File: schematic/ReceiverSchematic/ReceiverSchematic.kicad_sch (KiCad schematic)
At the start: 9 parts, among them Q1 BC547 (or similar NPN), Q2 S8550 (or similar PNP), U1 ESP32-DevKitC, U2 Ender 3 LCD (EXP3)

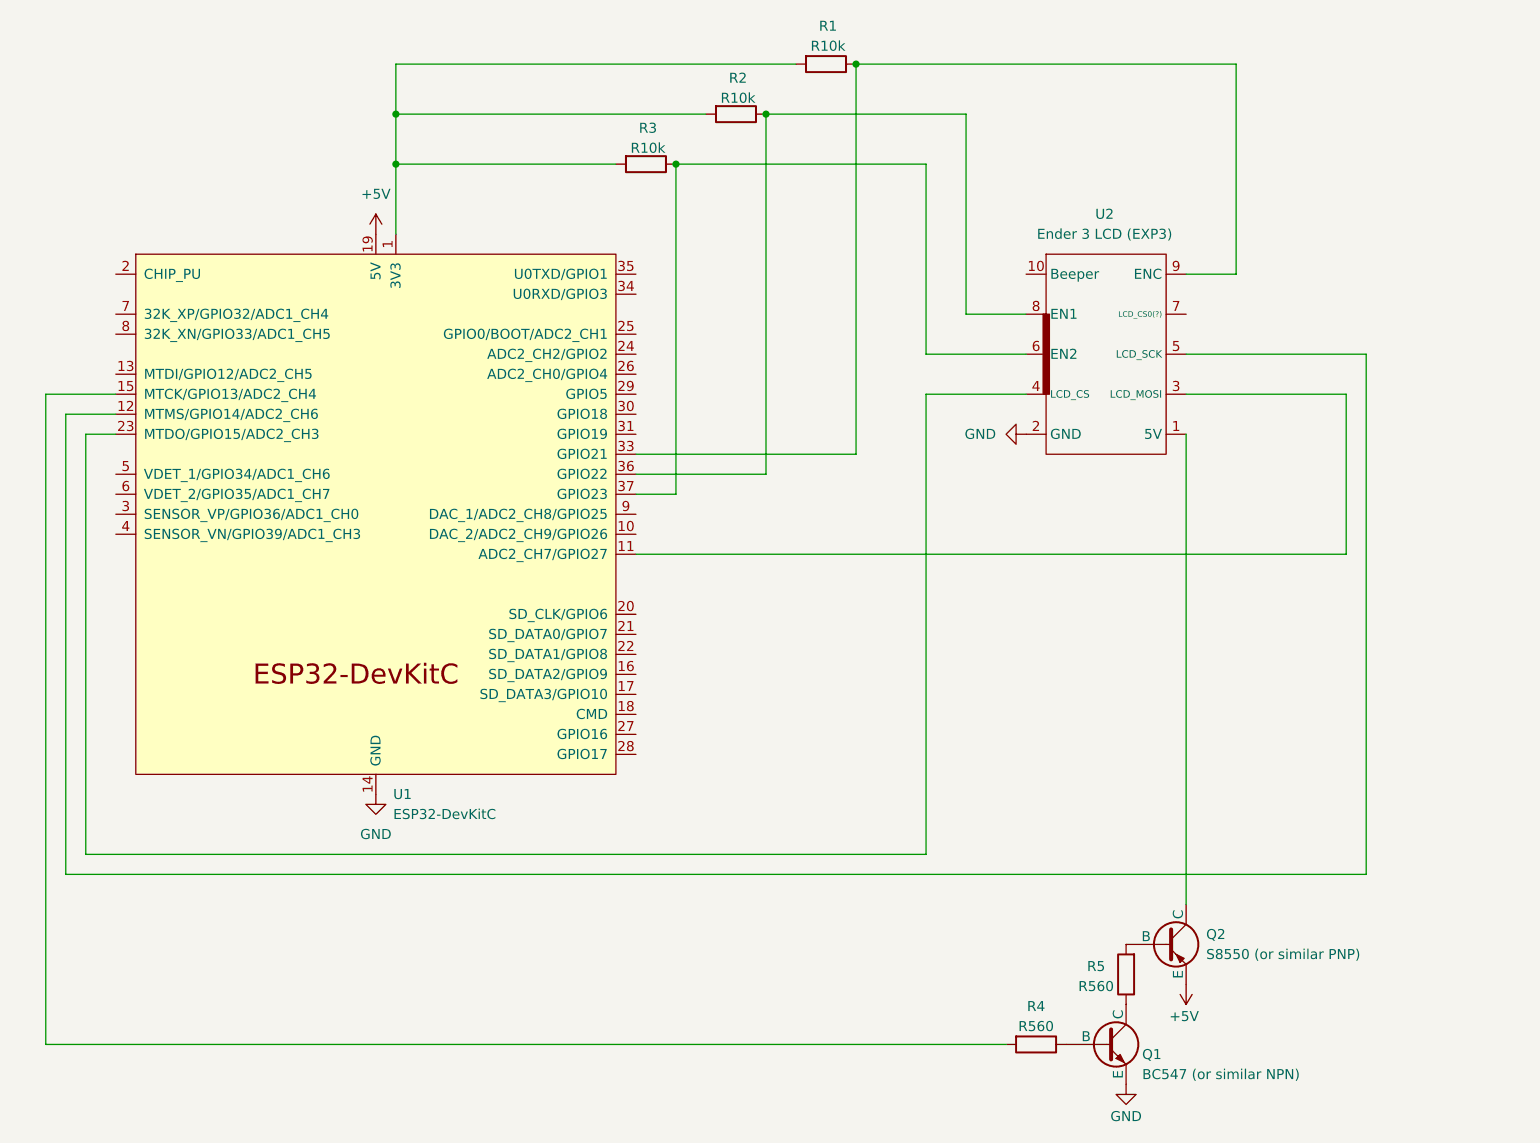
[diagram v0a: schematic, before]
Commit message: add LED ring to receiver schematic and CAD
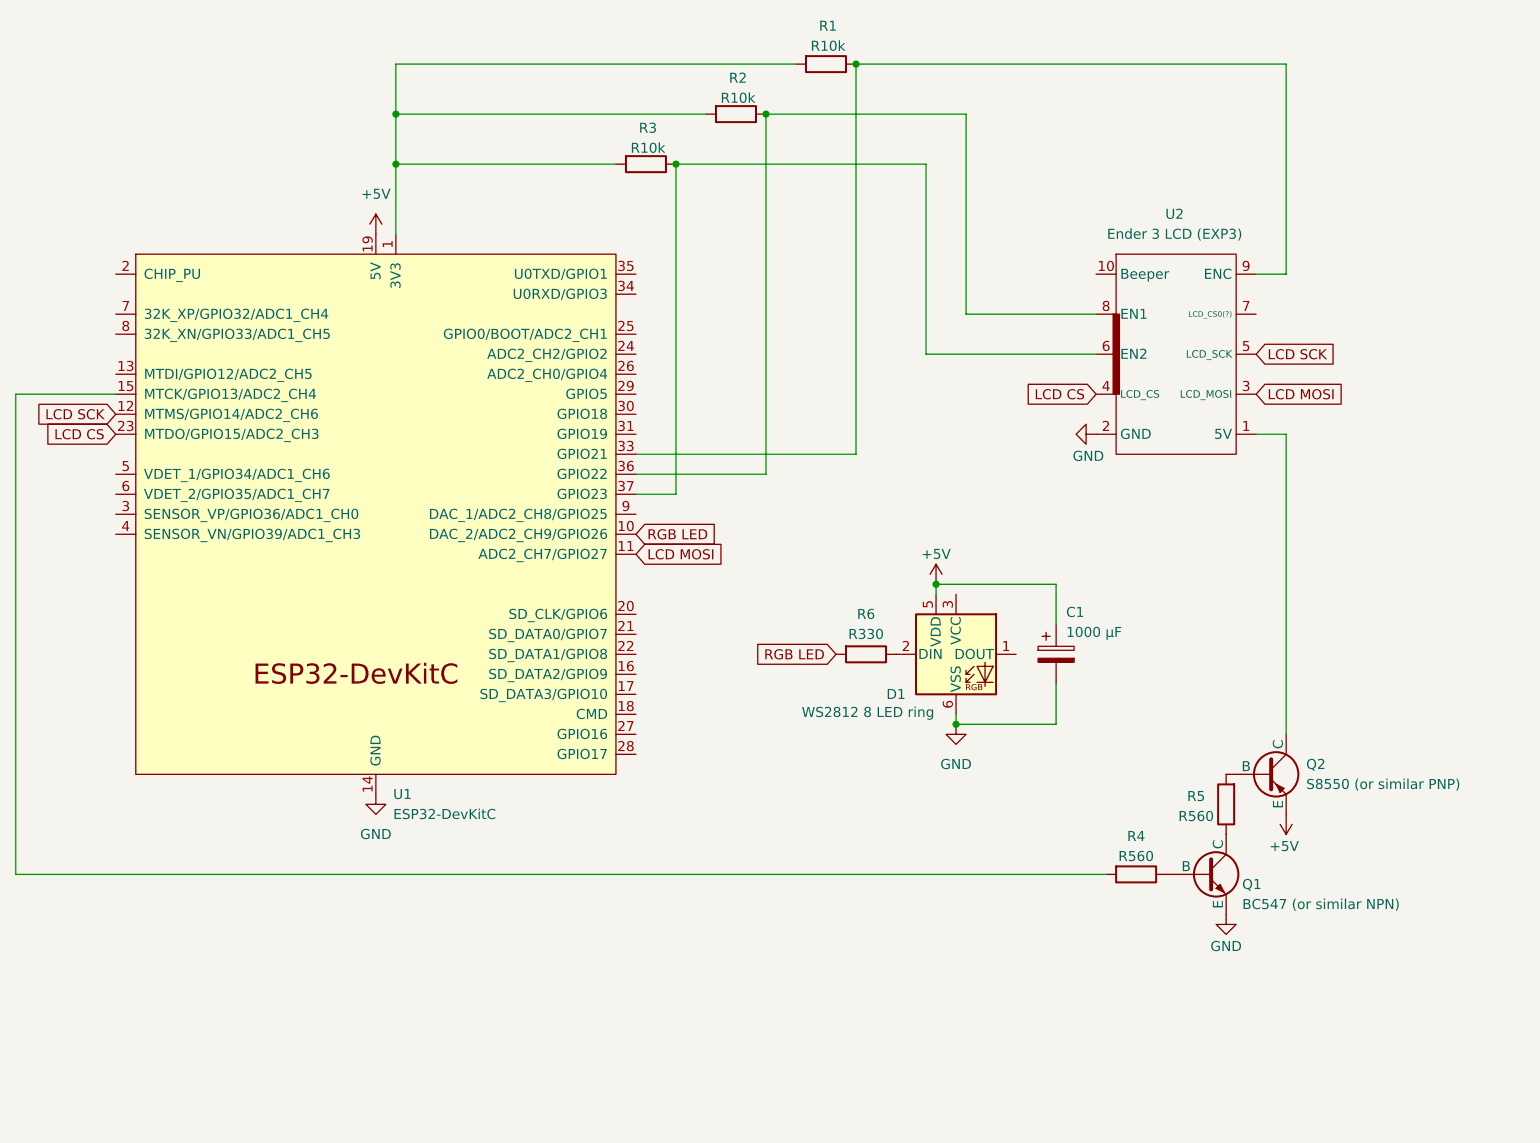
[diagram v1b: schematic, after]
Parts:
- added C1: 1000 μF, symbol Device:C_Polarized
- added D1: WS2812 8 LED ring, LED_SMD:LED_WS2812_PLCC6_5.0x5.0mm_P1.6mm, symbol LED:WS2812
- added R6: R330, symbol Device:R
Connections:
- net +5V: now also C1.1, D1.5 (VDD)
- net GND: now also C1.2, D1.6 (VSS)
- net RGB LED: now reaches U1.10 (DAC_2/ADC2_CH9/GPIO26)
- net RGB LED: now also R6.2
- net LCD MOSI: now reaches U1.11 (ADC2_CH7/GPIO27), U2.3 (LCD_MOSI)
- net LCD SCK: now reaches U1.12 (MTMS/GPIO14/ADC2_CH6), U2.5 (LCD_SCK)
- net LCD CS: now reaches U1.23 (MTDO/GPIO15/ADC2_CH3), U2.4 (LCD_CS)
- new net: D1.2 (DIN), R6.1
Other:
- moved on the sheet: Q1, Q2, R4, R5, U2
